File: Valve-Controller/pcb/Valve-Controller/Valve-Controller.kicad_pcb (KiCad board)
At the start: 0 parts

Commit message: Revert "Resolved recovery dev merge"
This reverts commit 81c4bbda93894cf9b120906f02d3dbab6bbd1e60, reversing
changes made to 220360569fc6c62025a0e7a68270d7f77f4a1f37.
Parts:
- added D1: D, Diode_SMD:D_SOD-123, F.Cu at (40.8, 32.1)
- added FID1: Fiducial, Fiducial:Fiducial_1mm_Mask2mm, F.Cu at (30.6, 38.0)
- added FID2: Fiducial, Fiducial:Fiducial_1mm_Mask2mm, F.Cu at (29.2, 27.8)
- added FID3: Fiducial, Fiducial:Fiducial_1mm_Mask2mm, F.Cu at (42.8, 37.8)
- added G***: LOGO, LOGO, B.Cu at (37.5, 34.3)
- added J1: Screw_Terminal_01x02, TerminalBlock_Phoenix:TerminalBlock_Phoenix_PT-1,5-2-3.5-H_1x02_P3.50mm_Horizontal, F.Cu at (45.5, 33.6)
- added J2: Conn_01x03_Socket, Connector_PinSocket_2.00mm:PinSocket_1x03_P2.00mm_Vertical, F.Cu at (25.7, 29.6)
- added Q1: SiS454DN, Package_SO:Vishay_PowerPAK_1212-8_Single, F.Cu at (36.9, 30.9)
- added R1: 3.3K, Resistor_SMD:R_0603_1608Metric_Pad0.98x0.95mm_HandSolder, F.Cu at (32.8, 29.8)
- added R2: 1K, Resistor_SMD:R_0603_1608Metric_Pad0.98x0.95mm_HandSolder, F.Cu at (32.8, 31.9)
- added R3: 100K, Resistor_SMD:R_0603_1608Metric_Pad0.98x0.95mm_HandSolder, F.Cu at (36.4, 26.7)
- added R4: 27K, Resistor_SMD:R_0603_1608Metric_Pad0.98x0.95mm_HandSolder, F.Cu at (36.4, 24.3)
- added TP1: TestPoint, TestPoint:TestPoint_Loop_D2.54mm_Drill1.5mm_Beaded, F.Cu at (31.9, 25.3)
- added TP2: TestPoint, TestPoint:TestPoint_Loop_D2.54mm_Drill1.5mm_Beaded, F.Cu at (41.4, 25.3)
- added TP3: TestPoint, TestPoint:TestPoint_Loop_D2.54mm_Drill1.5mm_Beaded, F.Cu at (45.5, 25.3)
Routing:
- net +12V: track 0.00 -> 20.4 mm
- net /ValveController/Output: track 0.00 -> 17.9 mm
- net /ValveController/Input: track 0.00 -> 13.4 mm
- net Net-(R3-Pad2): track 0.00 -> 2.37 mm
- net Net-(Q1-G): track 0.00 -> 1.75 mm
- added copper zone on F.Cu, net GNDD
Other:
- copper layers 0 -> 2
- board text added: "Valve Controller Rev. 1"
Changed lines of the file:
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@@
-(kicad_pcb (version 20240108) (generator "pcbnew") (generator_version "8.0")
-)
 (kicad_pcb
 	(version 20240108)
@@
 			)
 		)
-		(property "Datasheet" "https://www.onsemi.com/pdf/datasheet/mmsd4148t1-d.pdf"
+		(property "Datasheet" ""
 			(at 0 0 90)
 			(unlocked yes)
@@
 			)
 		)
-		(property "Purchase" "https://www.digikey.com/en/products/detail/onsemi/MMSD4148T1G/919705"
-			(at 0 0 90)
-			(unlocked yes)
-			(layer "F.Fab")
-			(hide yes)
-			(effects
-				(font
-					(size 1 1)
-					(thickness 0.15)
-				)
-			)
-		)
 		(property ki_fp_filters "TO-???* *_Diode_* *SingleDiode* D_*")
 		(sheetname "ValveController")
@@
 		)
 	)
-	(footprint "Connector_PinSocket_2.54mm:PinSocket_1x03_P2.54mm_Vertical"
+	(footprint "Connector_PinSocket_2.00mm:PinSocket_1x03_P2.00mm_Vertical"
 		(layer "F.Cu")
-		(at 25.908 28.956)
-		(descr "Through hole straight socket strip, 1x03, 2.54mm pitch, single row (from Kicad 4.0.7), script generated")
-		(tags "Through hole socket strip THT 1x03 2.54mm single row")
+		(at 25.654 29.623)
+		(descr "Through hole straight socket strip, 1x03, 2.00mm pitch, single row (from Kicad 4.0.7), script generated")
+		(tags "Through hole socket strip THT 1x03 2.00mm single row")
 		(property "Reference" "J2"
-			(at 0 -2.77 0)
+			(at 0 -2.318 0)
 			(layer "F.SilkS")
 			(effects
@@
 		)
 		(property "Value" "Conn_01x03_Socket"
-			(at 0 7.85 0)
+			(at 0 6.5 0)
 			(layer "F.Fab")
 			(effects
@@
 			)
 		)
-		(property "Footprint" "Connector_PinSocket_2.54mm:PinSocket_1x03_P2.54mm_Vertical"
+		(property "Footprint" "Connector_PinSocket_2.00mm:PinSocket_1x03_P2.00mm_Vertical"
 			(at 0 0 0)
 			(unlocked yes)
@@
 		(attr through_hole)
 		(fp_line
-			(start -1.33 1.27)
-			(end -1.33 6.41)
+			(start -1.06 1)
+			(end -1.06 5.06)
 			(stroke
 				(width 0.12)
@@
 		)
 		(fp_line
-			(start -1.33 1.27)
-			(end 1.33 1.27)
+			(start -1.06 1)
+			(end 1.06 1)
 			(stroke
 				(width 0.12)
@@
 		)
 		(fp_line
-			(start -1.33 6.41)
-			(end 1.33 6.41)
+			(start -1.06 5.06)
+			(end 1.06 5.06)
 			(stroke
 				(width 0.12)
@@
 		)
 		(fp_line
-			(start 0 -1.33)
-			(end 1.33 -1.33)
+			(start 0 -1.06)
+			(end 1.06 -1.06)
 			(stroke
 				(width 0.12)
@@
 		)
 		(fp_line
-			(start 1.33 -1.33)
-			(end 1.33 0)
+			(start 1.06 -1.06)
+			(end 1.06 0)
 			(stroke
 				(width 0.12)
@@
 		)
 		(fp_line
-			(start 1.33 1.27)
-			(end 1.33 6.41)
+			(start 1.06 1)
+			(end 1.06 5.06)
 			(stroke
 				(width 0.12)
@@
 		)
 		(fp_line
-			(start -1.8 -1.8)
-			(end 1.75 -1.8)
+			(start -1.5 -1.5)
+			(end 1.5 -1.5)
 			(stroke
 				(width 0.05)
@@
 		)
 		(fp_line
-			(start -1.8 6.85)
-			(end -1.8 -1.8)
+			(start -1.5 5.5)
+			(end -1.5 -1.5)
 			(stroke
 				(width 0.05)
@@
 		)
 		(fp_line
-			(start 1.75 -1.8)
-			(end 1.75 6.85)
+			(start 1.5 -1.5)
+			(end 1.5 5.5)
 			(stroke
 				(width 0.05)
@@
 		)
 		(fp_line
-			(start 1.75 6.85)
-			(end -1.8 6.85)
+			(start 1.5 5.5)
+			(end -1.5 5.5)
 			(stroke
 				(width 0.05)
@@
 		)
 		(fp_line
-			(start -1.27 -1.27)
-			(end 0.635 -1.27)
+			(start -1 -1)
+			(end 0.5 -1)
 			(stroke
 				(width 0.1)
@@
 		)
 		(fp_line
-			(start -1.27 6.35)
-			(end -1.27 -1.27)
+			(start -1 5)
+			(end -1 -1)
 			(stroke
 				(width 0.1)
@@
 		)
 		(fp_line
-			(start 0.635 -1.27)
-			(end 1.27 -0.635)
+			(start 0.5 -1)
+			(end 1 -0.5)
 			(stroke
 				(width 0.1)
@@
 		)
 		(fp_line
-			(start 1.27 -0.635)
-			(end 1.27 6.35)
+			(start 1 -0.5)
+			(end 1 5)
 			(stroke
 				(width 0.1)
@@
 		)
 		(fp_line
-			(start 1.27 6.35)
-			(end -1.27 6.35)
+			(start 1 5)
+			(end -1 5)
 			(stroke
 				(width 0.1)
@@
 		)
 		(fp_text user "${REFERENCE}"
-			(at 0 2.54 90)
+			(at 0 2 90)
 			(layer "F.Fab")
 			(effects
@@
 		(pad "1" thru_hole rect
 			(at 0 0)
-			(size 1.7 1.7)
-			(drill 1)
+			(size 1.35 1.35)
+			(drill 0.8)
 			(layers "*.Cu" "*.Mask")
 			(remove_unused_layers no)
@@
 		)
 		(pad "2" thru_hole oval
-			(at 0 2.54)
-			(size 1.7 1.7)
-			(drill 1)
+			(at 0 2)
+			(size 1.35 1.35)
+			(drill 0.8)
 			(layers "*.Cu" "*.Mask")
 			(remove_unused_layers no)
@@
 		)
 		(pad "3" thru_hole oval
-			(at 0 5.08)
-			(size 1.7 1.7)
-			(drill 1)
+			(at 0 4)
+			(size 1.35 1.35)
+			(drill 0.8)
 			(layers "*.Cu" "*.Mask")
 			(remove_unused_layers no)
@@
 			(pintype "passive")
 		)
-		(model "${KICAD8_3DMODEL_DIR}/Connector_PinSocket_2.54mm.3dshapes/PinSocket_1x03_P2.54mm_Vertical.wrl"
+		(model "${KICAD8_3DMODEL_DIR}/Connector_PinSocket_2.00mm.3dshapes/PinSocket_1x03_P2.00mm_Vertical.wrl"
 			(offset
 				(xyz 0 0 0)
@@
 	)
 	(segment
-		(start 31.933 33.599)
-		(end 31.496 34.036)
-		(width 1.016)
-		(layer "F.Cu")
-		(net 1)
-	)
-	(segment
-		(start 45.373 34.333)
-		(end 45.466 34.24)
+		(start 45.466 33.599)
+		(end 25.964 33.599)
 		(width 1.016)
 		(layer "F.Cu")
@@
 	)
 	(segment
-		(start 31.496 34.036)
-		(end 25.908 34.036)
+		(start 25.964 33.599)
+		(end 25.908 33.655)
 		(width 1.016)
 		(layer "F.Cu")
@@
 	)
 	(segment
-		(start 45.466 33.599)
-		(end 31.933 33.599)
+		(start 45.373 34.333)
+		(end 45.466 34.24)
 		(width 1.016)
 		(layer "F.Cu")

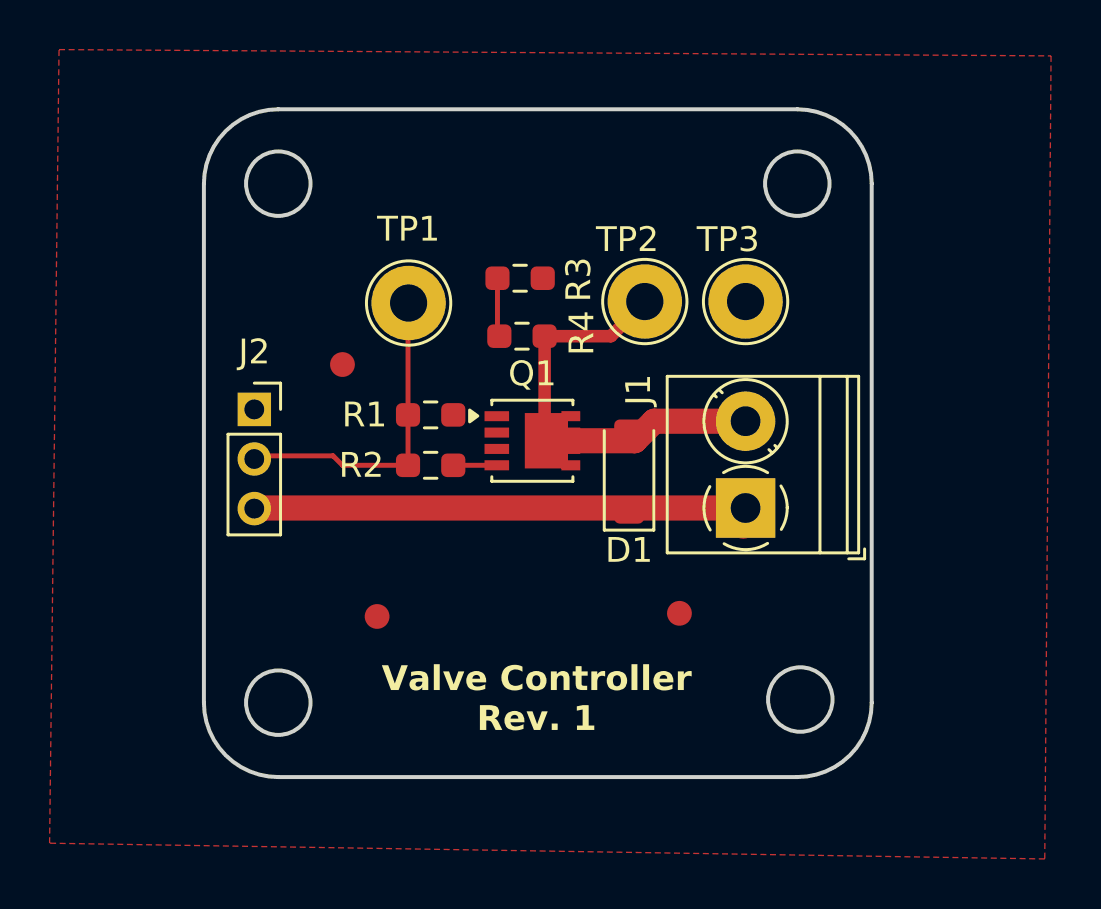
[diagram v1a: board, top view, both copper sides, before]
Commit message: Resized pin socket pitch to 2.54mm
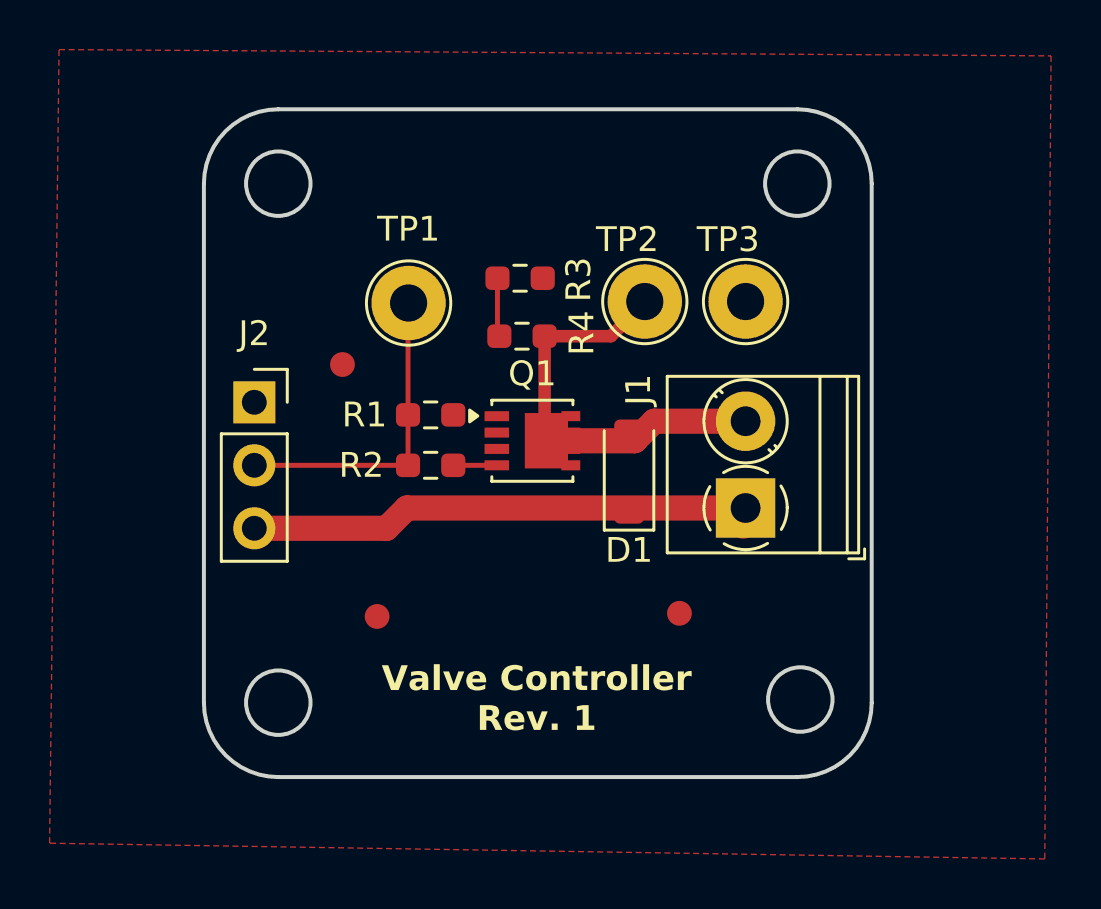
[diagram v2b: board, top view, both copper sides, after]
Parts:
- J2: footprint Connector_PinSocket_2.00mm:PinSocket_1x03_P2.00mm_Vertical -> Connector_PinSocket_2.54mm:PinSocket_1x03_P2.54mm_Vertical
- moved J2 0.29 mm to (25.7, 29.3)
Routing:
- net +12V: track 20.4 -> 20.9 mm
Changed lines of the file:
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@@
 			)
 		)
-		(property "Datasheet" ""
+		(property "Datasheet" "https://www.onsemi.com/pdf/datasheet/mmsd4148t1-d.pdf"
 			(at 0 0 90)
 			(unlocked yes)
@@
 			)
 		)
+		(property "Purchase" "https://www.digikey.com/en/products/detail/onsemi/MMSD4148T1G/919705"
+			(at 0 0 90)
+			(unlocked yes)
+			(layer "F.Fab")
+			(hide yes)
+			(effects
+				(font
+					(size 1 1)
+					(thickness 0.15)
+				)
+			)
+		)
 		(property ki_fp_filters "TO-???* *_Diode_* *SingleDiode* D_*")
 		(sheetname "ValveController")
@@
 		)
 	)
-	(footprint "Connector_PinSocket_2.00mm:PinSocket_1x03_P2.00mm_Vertical"
+	(footprint "Connector_PinSocket_2.54mm:PinSocket_1x03_P2.54mm_Vertical"
 		(layer "F.Cu")
-		(at 25.654 29.623)
-		(descr "Through hole straight socket strip, 1x03, 2.00mm pitch, single row (from Kicad 4.0.7), script generated")
-		(tags "Through hole socket strip THT 1x03 2.00mm single row")
+		(at 25.654 29.337)
+		(descr "Through hole straight socket strip, 1x03, 2.54mm pitch, single row (from Kicad 4.0.7), script generated")
+		(tags "Through hole socket strip THT 1x03 2.54mm single row")
 		(property "Reference" "J2"
-			(at 0 -2.318 0)
+			(at 0 -2.77 0)
 			(layer "F.SilkS")
 			(effects
@@
 		)
 		(property "Value" "Conn_01x03_Socket"
-			(at 0 6.5 0)
+			(at 0 7.85 0)
 			(layer "F.Fab")
 			(effects
@@
 			)
 		)
-		(property "Footprint" "Connector_PinSocket_2.00mm:PinSocket_1x03_P2.00mm_Vertical"
+		(property "Footprint" "Connector_PinSocket_2.54mm:PinSocket_1x03_P2.54mm_Vertical"
 			(at 0 0 0)
 			(unlocked yes)
@@
 		(attr through_hole)
 		(fp_line
-			(start -1.06 1)
-			(end -1.06 5.06)
+			(start -1.33 1.27)
+			(end -1.33 6.41)
 			(stroke
 				(width 0.12)
@@
 		)
 		(fp_line
-			(start -1.06 1)
-			(end 1.06 1)
+			(start -1.33 1.27)
+			(end 1.33 1.27)
 			(stroke
 				(width 0.12)
@@
 		)
 		(fp_line
-			(start -1.06 5.06)
-			(end 1.06 5.06)
+			(start -1.33 6.41)
+			(end 1.33 6.41)
 			(stroke
 				(width 0.12)
@@
 		)
 		(fp_line
-			(start 0 -1.06)
-			(end 1.06 -1.06)
+			(start 0 -1.33)
+			(end 1.33 -1.33)
 			(stroke
 				(width 0.12)
@@
 		)
 		(fp_line
-			(start 1.06 -1.06)
-			(end 1.06 0)
+			(start 1.33 -1.33)
+			(end 1.33 0)
 			(stroke
 				(width 0.12)
@@
 		)
 		(fp_line
-			(start 1.06 1)
-			(end 1.06 5.06)
+			(start 1.33 1.27)
+			(end 1.33 6.41)
 			(stroke
 				(width 0.12)
@@
 		)
 		(fp_line
-			(start -1.5 -1.5)
-			(end 1.5 -1.5)
+			(start -1.8 -1.8)
+			(end 1.75 -1.8)
 			(stroke
 				(width 0.05)
@@
 		)
 		(fp_line
-			(start -1.5 5.5)
-			(end -1.5 -1.5)
+			(start -1.8 6.85)
+			(end -1.8 -1.8)
 			(stroke
 				(width 0.05)
@@
 		)
 		(fp_line
-			(start 1.5 -1.5)
-			(end 1.5 5.5)
+			(start 1.75 -1.8)
+			(end 1.75 6.85)
 			(stroke
 				(width 0.05)
@@
 		)
 		(fp_line
-			(start 1.5 5.5)
-			(end -1.5 5.5)
+			(start 1.75 6.85)
+			(end -1.8 6.85)
 			(stroke
 				(width 0.05)
@@
 		)
 		(fp_line
-			(start -1 -1)
-			(end 0.5 -1)
+			(start -1.27 -1.27)
+			(end 0.635 -1.27)
 			(stroke
 				(width 0.1)
@@
 		)
 		(fp_line
-			(start -1 5)
-			(end -1 -1)
+			(start -1.27 6.35)
+			(end -1.27 -1.27)
 			(stroke
 				(width 0.1)
@@
 		)
 		(fp_line
-			(start 0.5 -1)
-			(end 1 -0.5)
+			(start 0.635 -1.27)
+			(end 1.27 -0.635)
 			(stroke
 				(width 0.1)
@@
 		)
 		(fp_line
-			(start 1 -0.5)
-			(end 1 5)
+			(start 1.27 -0.635)
+			(end 1.27 6.35)
 			(stroke
 				(width 0.1)
@@
 		)
 		(fp_line
-			(start 1 5)
-			(end -1 5)
+			(start 1.27 6.35)
+			(end -1.27 6.35)
 			(stroke
 				(width 0.1)
@@
 		)
 		(fp_text user "${REFERENCE}"
-			(at 0 2 90)
+			(at 0 2.54 90)
 			(layer "F.Fab")
 			(effects
@@
 		(pad "1" thru_hole rect
 			(at 0 0)
-			(size 1.35 1.35)
-			(drill 0.8)
+			(size 1.7 1.7)
+			(drill 1)
 			(layers "*.Cu" "*.Mask")
 			(remove_unused_layers no)
@@
 		)
 		(pad "2" thru_hole oval
-			(at 0 2)
-			(size 1.35 1.35)
-			(drill 0.8)
+			(at 0 2.54)
+			(size 1.7 1.7)
+			(drill 1)
 			(layers "*.Cu" "*.Mask")
 			(remove_unused_layers no)
@@
 		)
 		(pad "3" thru_hole oval
-			(at 0 4)
-			(size 1.35 1.35)
-			(drill 0.8)
+			(at 0 5.08)
+			(size 1.7 1.7)
+			(drill 1)
 			(layers "*.Cu" "*.Mask")
 			(remove_unused_layers no)
@@
 			(pintype "passive")
 		)
-		(model "${KICAD8_3DMODEL_DIR}/Connector_PinSocket_2.00mm.3dshapes/PinSocket_1x03_P2.00mm_Vertical.wrl"
+		(model "${KICAD8_3DMODEL_DIR}/Connector_PinSocket_2.54mm.3dshapes/PinSocket_1x03_P2.54mm_Vertical.wrl"
 			(offset
 				(xyz 0 0 0)
@@
 	)
 	(segment
-		(start 45.466 33.599)
-		(end 25.964 33.599)
+		(start 31.806 33.599)
+		(end 30.988 34.417)
 		(width 1.016)
 		(layer "F.Cu")
@@
 	)
 	(segment
-		(start 25.964 33.599)
-		(end 25.908 33.655)
+		(start 45.373 34.333)
+		(end 45.466 34.24)
 		(width 1.016)
 		(layer "F.Cu")
@@
 	)
 	(segment
-		(start 45.373 34.333)
-		(end 45.466 34.24)
+		(start 45.466 33.599)
+		(end 31.806 33.599)
+		(width 1.016)
+		(layer "F.Cu")
+		(net 1)
+	)
+	(segment
+		(start 30.988 34.417)
+		(end 25.654 34.417)
 		(width 1.016)
 		(layer "F.Cu")
@@
 	)
 	(segment
-		(start 28.829 31.496)
-		(end 25.781 31.496)
-		(width 0.2)
-		(layer "F.Cu")
-		(net 5)
-	)
-	(segment
 		(start 31.8535 31.877)
-		(end 29.21 31.877)
-		(width 0.2)
-		(layer "F.Cu")
-		(net 5)
-	)
-	(segment
-		(start 29.21 31.877)
-		(end 28.829 31.496)
+		(end 25.908 31.877)
 		(width 0.2)
 		(layer "F.Cu")
@@
 	)
 	(segment
-		(start 25.781 31.496)
+		(start 25.908 31.877)
 		(end 25.654 31.623)
 		(width 0.2)
